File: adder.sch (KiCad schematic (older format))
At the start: 31 parts

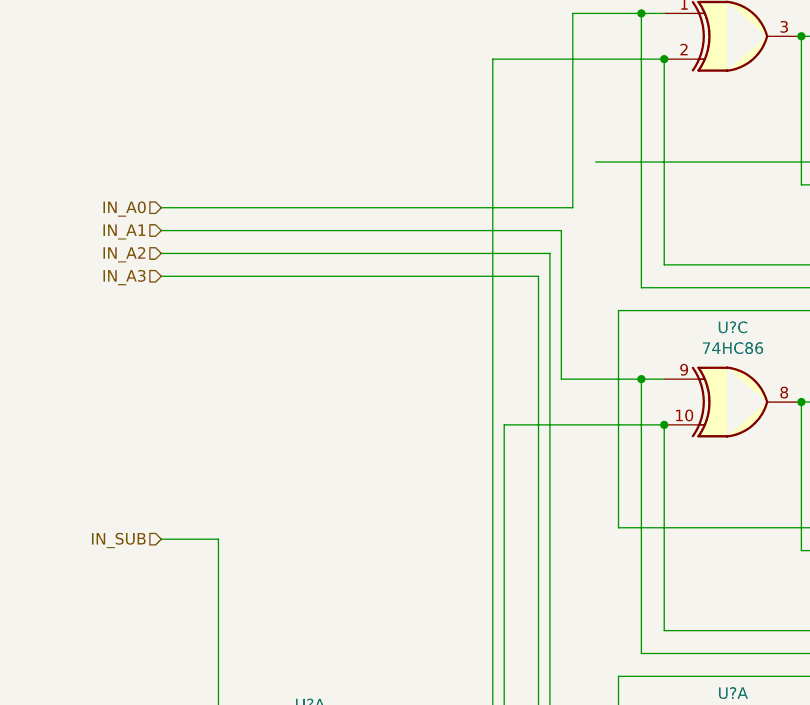
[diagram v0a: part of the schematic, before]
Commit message: Add missing wire in adder
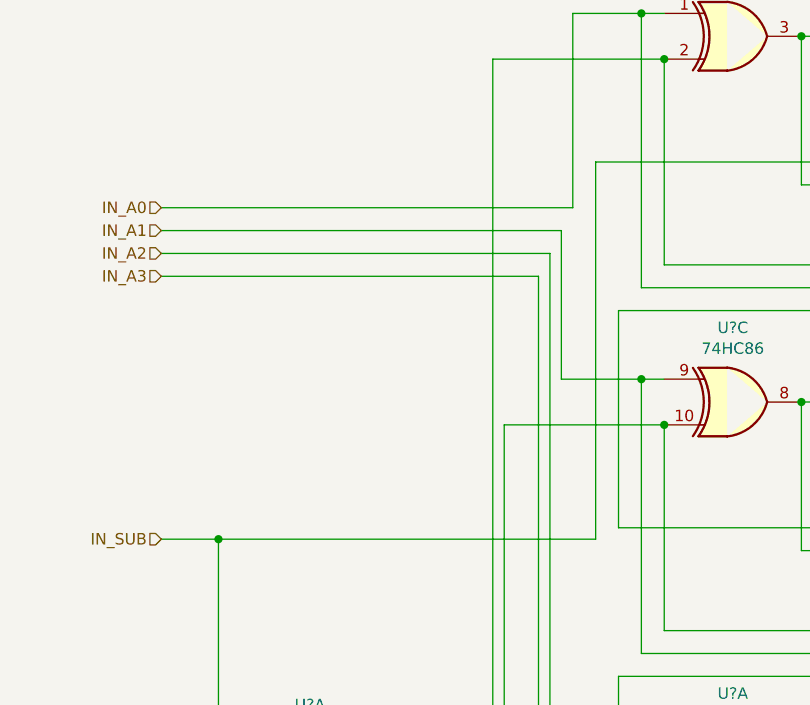
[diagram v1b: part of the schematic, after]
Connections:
- net IN_SUB: now also U?.1 (1A), U?.5
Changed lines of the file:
@@
 	1    0    0    -1
 $EndComp
+Wire Wire Line
+	2650 3500 4300 3500
+Wire Wire Line
+	4300 3500 4300 1850
+Connection ~ 2650 3500
 $EndSCHEMATC

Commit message: Anotate alu
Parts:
- gave numbers to parts that had none: 6

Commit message: tiny fixes in annotation
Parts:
- added unit 5 of U16
- gave numbers to parts that had none: 1
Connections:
- net +5V: now also U16.14 (VCC)
- net GND: now also U16.7 (GND)
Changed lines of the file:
@@
 AR Path="/6085805F" Ref="#PWR?"  Part="1"
 AR Path="/5FEB4D4D/6085805F" Ref="#PWR?"  Part="1"
-AR Path="/600A4AF3/600A5215/6085805F" Ref="#PWR?"  Part="1"
-F 0 "#PWR?" H 7600 2000 50  0001 C CNN
+AR Path="/600A4AF3/600A5215/6085805F" Ref="#PWR0112"  Part="1"
+F 0 "#PWR0112" H 7600 2000 50  0001 C CNN
 F 1 "GND" V 7605 2122 50  0000 R CNN
 F 2 "" H 7600 2250 50  0001 C CNN
@@
 AR Path="/60858065" Ref="#PWR?"  Part="1"
 AR Path="/5FEB4D4D/60858065" Ref="#PWR?"  Part="1"
-AR Path="/600A4AF3/600A5215/60858065" Ref="#PWR?"  Part="1"
-F 0 "#PWR?" H 7600 1100 50  0001 C CNN
+AR Path="/600A4AF3/600A5215/60858065" Ref="#PWR0115"  Part="1"
+F 0 "#PWR0115" H 7600 1100 50  0001 C CNN
 F 1 "+5V" V 7615 1378 50  0000 L CNN
 F 2 "" H 7600 1250 50  0001 C CNN
@@
 AR Path="/60858072" Ref="#PWR?"  Part="1"
 AR Path="/5FEB4D4D/60858072" Ref="#PWR?"  Part="1"
-AR Path="/600A4AF3/600A5215/60858072" Ref="#PWR?"  Part="1"
-F 0 "#PWR?" H 9000 2800 50  0001 C CNN
+AR Path="/600A4AF3/600A5215/60858072" Ref="#PWR0116"  Part="1"
+F 0 "#PWR0116" H 9000 2800 50  0001 C CNN
 F 1 "GND" V 9005 2922 50  0000 R CNN
 F 2 "" H 9000 3050 50  0001 C CNN
@@
 AR Path="/60858078" Ref="#PWR?"  Part="1"
 AR Path="/5FEB4D4D/60858078" Ref="#PWR?"  Part="1"
-AR Path="/600A4AF3/600A5215/60858078" Ref="#PWR?"  Part="1"
-F 0 "#PWR?" H 9000 1900 50  0001 C CNN
+AR Path="/600A4AF3/600A5215/60858078" Ref="#PWR0117"  Part="1"
+F 0 "#PWR0117" H 9000 1900 50  0001 C CNN
 F 1 "+5V" V 9015 2178 50  0000 L CNN
 F 2 "" H 9000 2050 50  0001 C CNN
@@
 AR Path="/6085808C" Ref="#PWR?"  Part="1"
 AR Path="/5FEB4D4D/6085808C" Ref="#PWR?"  Part="1"
-AR Path="/600A4AF3/600A5215/6085808C" Ref="#PWR?"  Part="1"
-F 0 "#PWR?" H 7850 3950 50  0001 C CNN
+AR Path="/600A4AF3/600A5215/6085808C" Ref="#PWR0118"  Part="1"
+F 0 "#PWR0118" H 7850 3950 50  0001 C CNN
 F 1 "GND" V 7855 4072 50  0000 R CNN
 F 2 "" H 7850 4200 50  0001 C CNN
@@
 AR Path="/60858092" Ref="#PWR?"  Part="1"
 AR Path="/5FEB4D4D/60858092" Ref="#PWR?"  Part="1"
-AR Path="/600A4AF3/600A5215/60858092" Ref="#PWR?"  Part="1"
-F 0 "#PWR?" H 7850 3350 50  0001 C CNN
+AR Path="/600A4AF3/600A5215/60858092" Ref="#PWR0120"  Part="1"
+F 0 "#PWR0120" H 7850 3350 50  0001 C CNN
 F 1 "+5V" V 7865 3628 50  0000 L CNN
 F 2 "" H 7850 3500 50  0001 C CNN
@@
 AR Path="/608B570A" Ref="#PWR?"  Part="1"
 AR Path="/5FEB4D4D/608B570A" Ref="#PWR?"  Part="1"
-AR Path="/600A4AF3/600A5215/608B570A" Ref="#PWR?"  Part="1"
-F 0 "#PWR?" H 8300 5200 50  0001 C CNN
+AR Path="/600A4AF3/600A5215/608B570A" Ref="#PWR0135"  Part="1"
+F 0 "#PWR0135" H 8300 5200 50  0001 C CNN
 F 1 "GND" V 8305 5322 50  0000 R CNN
 F 2 "" H 8300 5450 50  0001 C CNN
@@
 AR Path="/608B5710" Ref="#PWR?"  Part="1"
 AR Path="/5FEB4D4D/608B5710" Ref="#PWR?"  Part="1"
-AR Path="/600A4AF3/600A5215/608B5710" Ref="#PWR?"  Part="1"
-F 0 "#PWR?" H 8300 4300 50  0001 C CNN
+AR Path="/600A4AF3/600A5215/608B5710" Ref="#PWR0136"  Part="1"
+F 0 "#PWR0136" H 8300 4300 50  0001 C CNN
 F 1 "+5V" V 8315 4578 50  0000 L CNN
 F 2 "" H 8300 4450 50  0001 C CNN
@@
 AR Path="/608BBB4D" Ref="#PWR?"  Part="1"
 AR Path="/5FEB4D4D/608BBB4D" Ref="#PWR?"  Part="1"
-AR Path="/600A4AF3/600A5215/608BBB4D" Ref="#PWR?"  Part="1"
-F 0 "#PWR?" H 1700 6500 50  0001 C CNN
+AR Path="/600A4AF3/600A5215/608BBB4D" Ref="#PWR0137"  Part="1"
+F 0 "#PWR0137" H 1700 6500 50  0001 C CNN
 F 1 "GND" V 1705 6622 50  0000 R CNN
 F 2 "" H 1700 6750 50  0001 C CNN
@@
 AR Path="/608BBB53" Ref="#PWR?"  Part="1"
 AR Path="/5FEB4D4D/608BBB53" Ref="#PWR?"  Part="1"
-AR Path="/600A4AF3/600A5215/608BBB53" Ref="#PWR?"  Part="1"
-F 0 "#PWR?" H 1700 5600 50  0001 C CNN
+AR Path="/600A4AF3/600A5215/608BBB53" Ref="#PWR0138"  Part="1"
+F 0 "#PWR0138" H 1700 5600 50  0001 C CNN
 F 1 "+5V" V 1715 5878 50  0000 L CNN
 F 2 "" H 1700 5750 50  0001 C CNN
@@
 AR Path="/608E9FF4" Ref="#PWR?"  Part="1"
 AR Path="/5FEB4D4D/608E9FF4" Ref="#PWR?"  Part="1"
-AR Path="/600A4AF3/600A5215/608E9FF4" Ref="#PWR?"  Part="1"
-F 0 "#PWR?" H 9050 5050 50  0001 C CNN
+AR Path="/600A4AF3/600A5215/608E9FF4" Ref="#PWR0139"  Part="1"
+F 0 "#PWR0139" H 9050 5050 50  0001 C CNN
 F 1 "GND" V 9055 5172 50  0000 R CNN
 F 2 "" H 9050 5300 50  0001 C CNN
@@
 AR Path="/608E9FFA" Ref="#PWR?"  Part="1"
 AR Path="/5FEB4D4D/608E9FFA" Ref="#PWR?"  Part="1"
-AR Path="/600A4AF3/600A5215/608E9FFA" Ref="#PWR?"  Part="1"
-F 0 "#PWR?" H 9050 4150 50  0001 C CNN
+AR Path="/600A4AF3/600A5215/608E9FFA" Ref="#PWR0140"  Part="1"
+F 0 "#PWR0140" H 9050 4150 50  0001 C CNN
 F 1 "+5V" V 9065 4428 50  0000 L CNN
 F 2 "" H 9050 4300 50  0001 C CNN
@@
 P 7100 5650
 AR Path="/5FEB4D4D/600EFDE5" Ref="U?"  Part="2"
-AR Path="/600A4AF3/600A5215/600EFDE5" Ref="U?"  Part="4"
-F 0 "U?" H 7100 5975 50  0000 C CNN
+AR Path="/600A4AF3/600A5215/600EFDE5" Ref="U16"  Part="4"
+F 0 "U16" H 7100 5975 50  0000 C CNN
 F 1 "74HC86" H 7100 5884 50  0000 C CNN
 F 2 "Package_SO:TSSOP-14_4.4x5mm_P0.65mm" H 7100 5650 50  0001 C CNN
@@
 	4300 3500 4300 1850
 Connection ~ 2650 3500
+$Comp
+L power:GND #PWR?
+U 1 1 60384320
+P 10150 4200
+AR Path="/60384320" Ref="#PWR?"  Part="1"
+AR Path="/5FEB4D4D/60384320" Ref="#PWR?"  Part="1"
+AR Path="/600A4AF3/600A5215/60384320" Ref="#PWR0200"  Part="1"
+F 0 "#PWR0200" H 10150 3950 50  0001 C CNN
+F 1 "GND" V 10155 4072 50  0000 R CNN
+F 2 "" H 10150 4200 50  0001 C CNN
+F 3 "" H 10150 4200 50  0001 C CNN
+	1    10150 4200
+	1    0    0    -1
+$EndComp
+$Comp
+L power:+5V #PWR?
+U 1 1 60384326
+P 10150 3200
+AR Path="/60384326" Ref="#PWR?"  Part="1"
+AR Path="/5FEB4D4D/60384326" Ref="#PWR?"  Part="1"
+AR Path="/600A4AF3/600A5215/60384326" Ref="#PWR0201"  Part="1"
+F 0 "#PWR0201" H 10150 3050 50  0001 C CNN
+F 1 "+5V" V 10165 3328 50  0000 L CNN
+F 2 "" H 10150 3200 50  0001 C CNN
+F 3 "" H 10150 3200 50  0001 C CNN
+	1    10150 3200
+	1    0    0    -1
+$EndComp
+$Comp
+L 74xx:74HC86 U?
+U 5 1 6038432D
+P 10150 3700
+AR Path="/5FEB4D4D/6038432D" Ref="U?"  Part="5"
+AR Path="/600A4AF3/600A5215/6038432D" Ref="U16"  Part="5"
+F 0 "U16" H 10380 3746 50  0000 L CNN
+F 1 "74HC86" H 10380 3655 50  0000 L CNN
+F 2 "Package_SO:TSSOP-14_4.4x5mm_P0.65mm" H 10150 3700 50  0001 C CNN
+F 3 "https://datasheet.lcsc.com/szlcsc/Texas-Instruments-TI-SN74AHC86PWR_C117522.pdf" H 10150 3700 50  0001 C CNN
+F 4 "C117522" H 10150 3700 50  0001 C CNN "LCSC"
+	5    10150 3700
+	1    0    0    -1
+$EndComp
 $EndSCHEMATC

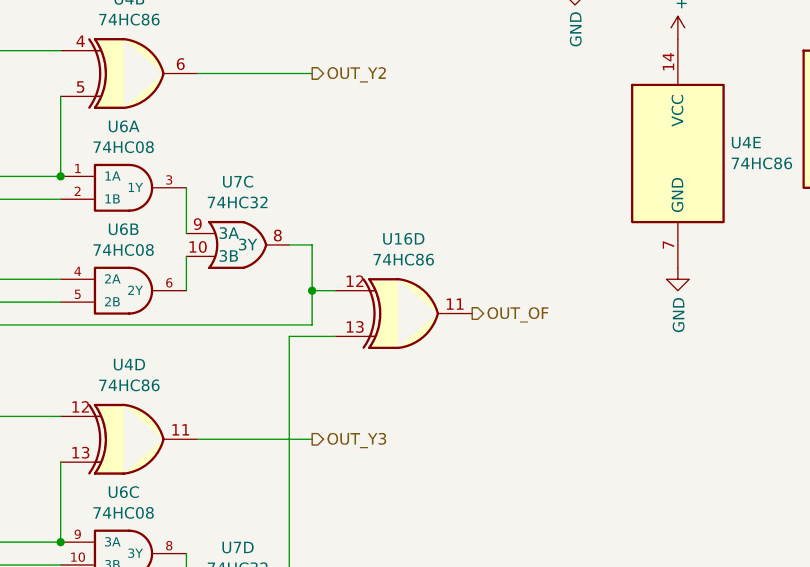
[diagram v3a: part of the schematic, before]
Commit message: exchanged a single AND
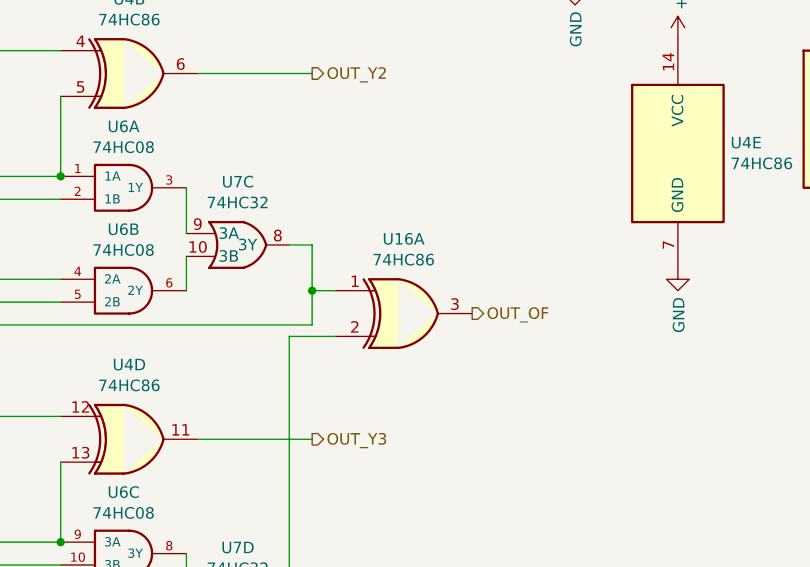
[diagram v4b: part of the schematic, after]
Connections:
- net OUT_OF: now also U16.3; no longer U16.11
- net at U4.13, U6.9 (3A), U7.8 (3Y): now also U16.1; no longer U16.12
- net at U7.11 (4Y): now also U16.2; no longer U16.13
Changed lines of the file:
@@
 $Comp
 L 74xx:74HC86 U?
-U 4 1 600EFDE5
+U 1 1 600EFDE5
 P 7100 5650
 AR Path="/5FEB4D4D/600EFDE5" Ref="U?"  Part="2"
-AR Path="/600A4AF3/600A5215/600EFDE5" Ref="U16"  Part="4"
+AR Path="/600A4AF3/600A5215/600EFDE5" Ref="U16"  Part="1"
 F 0 "U16" H 7100 5975 50  0000 C CNN
 F 1 "74HC86" H 7100 5884 50  0000 C CNN
@@
 F 3 "https://datasheet.lcsc.com/szlcsc/Texas-Instruments-TI-SN74AHC86PWR_C117522.pdf" H 7100 5650 50  0001 C CNN
 F 4 "C117522" H 7100 5650 50  0001 C CNN "LCSC"
-	4    7100 5650
+	1    7100 5650
 	1    0    0    -1
 $EndComp

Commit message: fixed some footprints
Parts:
- U5, U6, U7: footprint Housings_SOIC:SOIC-14_3.9x8.7mm_Pitch1.27mm -> Package_SO:SOIC-14_3.9x8.7mm_P1.27mm
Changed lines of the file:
@@
 F 0 "U6" H 5875 6967 50  0000 C CNN
 F 1 "74HC08" H 5875 6876 50  0000 C CNN
-F 2 "Housings_SOIC:SOIC-14_3.9x8.7mm_Pitch1.27mm" H 5850 6700 50  0001 C CNN
+F 2 "Package_SO:SOIC-14_3.9x8.7mm_P1.27mm" H 5850 6700 50  0001 C CNN
 F 3 "https://datasheet.lcsc.com/szlcsc/Nexperia-74HC08D-653_C5593.pdf" H 5850 6700 50  0001 C CNN
 F 4 "C5593" H 5850 6700 50  0001 C CNN "LCSC"
@@
 F 0 "U5" H 5875 3767 50  0000 C CNN
 F 1 "74HC08" H 5875 3676 50  0000 C CNN
-F 2 "Housings_SOIC:SOIC-14_3.9x8.7mm_Pitch1.27mm" H 5850 3500 50  0001 C CNN
+F 2 "Package_SO:SOIC-14_3.9x8.7mm_P1.27mm" H 5850 3500 50  0001 C CNN
 F 3 "https://datasheet.lcsc.com/szlcsc/Nexperia-74HC08D-653_C5593.pdf" H 5850 3500 50  0001 C CNN
 F 4 "C5593" H 5850 3500 50  0001 C CNN "LCSC"
@@
 F 0 "U7" H 6375 4025 50  0000 C CNN
 F 1 "74HC32" H 6375 3934 50  0000 C CNN
-F 2 "Housings_SOIC:SOIC-14_3.9x8.7mm_Pitch1.27mm" H 5850 3950 50  0001 C CNN
+F 2 "Package_SO:SOIC-14_3.9x8.7mm_P1.27mm" H 5850 3950 50  0001 C CNN
 F 3 "https://datasheet.lcsc.com/szlcsc/Nexperia-74HC32D-653_C5632.pdf" H 5850 3950 50  0001 C CNN
 F 4 "C5632" H 6400 3750 50  0001 C CNN "LCSC"
@@
 F 0 "U7" H 6375 2425 50  0000 C CNN
 F 1 "74HC32" H 6375 2334 50  0000 C CNN
-F 2 "Housings_SOIC:SOIC-14_3.9x8.7mm_Pitch1.27mm" H 5850 2350 50  0001 C CNN
+F 2 "Package_SO:SOIC-14_3.9x8.7mm_P1.27mm" H 5850 2350 50  0001 C CNN
 F 3 "https://datasheet.lcsc.com/szlcsc/Nexperia-74HC32D-653_C5632.pdf" H 5850 2350 50  0001 C CNN
 F 4 "C5632" H 6400 2150 50  0001 C CNN "LCSC"
@@
 F 0 "U5" H 5875 2617 50  0000 C CNN
 F 1 "74HC08" H 5875 2526 50  0000 C CNN
-F 2 "Housings_SOIC:SOIC-14_3.9x8.7mm_Pitch1.27mm" H 5850 2350 50  0001 C CNN
+F 2 "Package_SO:SOIC-14_3.9x8.7mm_P1.27mm" H 5850 2350 50  0001 C CNN
 F 3 "https://datasheet.lcsc.com/szlcsc/Nexperia-74HC08D-653_C5593.pdf" H 5850 2350 50  0001 C CNN
 F 4 "C5593" H 5850 2350 50  0001 C CNN "LCSC"
@@
 F 0 "U5" H 5875 2167 50  0000 C CNN
 F 1 "74HC08" H 5875 2076 50  0000 C CNN
-F 2 "Housings_SOIC:SOIC-14_3.9x8.7mm_Pitch1.27mm" H 5850 1900 50  0001 C CNN
+F 2 "Package_SO:SOIC-14_3.9x8.7mm_P1.27mm" H 5850 1900 50  0001 C CNN
 F 3 "https://datasheet.lcsc.com/szlcsc/Nexperia-74HC08D-653_C5593.pdf" H 5850 1900 50  0001 C CNN
 F 4 "C5593" H 5850 1900 50  0001 C CNN "LCSC"
@@
 F 0 "U6" H 5875 5817 50  0000 C CNN
 F 1 "74HC08" H 5875 5726 50  0000 C CNN
-F 2 "Housings_SOIC:SOIC-14_3.9x8.7mm_Pitch1.27mm" H 5850 5550 50  0001 C CNN
+F 2 "Package_SO:SOIC-14_3.9x8.7mm_P1.27mm" H 5850 5550 50  0001 C CNN
 F 3 "https://datasheet.lcsc.com/szlcsc/Nexperia-74HC08D-653_C5593.pdf" H 5850 5550 50  0001 C CNN
 F 4 "C5593" H 5850 5550 50  0001 C CNN "LCSC"
@@
 F 0 "U6" H 5875 5367 50  0000 C CNN
 F 1 "74HC08" H 5875 5276 50  0000 C CNN
-F 2 "Housings_SOIC:SOIC-14_3.9x8.7mm_Pitch1.27mm" H 5850 5100 50  0001 C CNN
+F 2 "Package_SO:SOIC-14_3.9x8.7mm_P1.27mm" H 5850 5100 50  0001 C CNN
 F 3 "https://datasheet.lcsc.com/szlcsc/Nexperia-74HC08D-653_C5593.pdf" H 5850 5100 50  0001 C CNN
 F 4 "C5593" H 5850 5100 50  0001 C CNN "LCSC"
@@
 F 0 "U5" H 9230 2596 50  0000 L CNN
 F 1 "74HC08" H 9230 2505 50  0000 L CNN
-F 2 "Housings_SOIC:SOIC-14_3.9x8.7mm_Pitch1.27mm" H 9000 2550 50  0001 C CNN
+F 2 "Package_SO:SOIC-14_3.9x8.7mm_P1.27mm" H 9000 2550 50  0001 C CNN
 F 3 "https://datasheet.lcsc.com/szlcsc/Nexperia-74HC08D-653_C5593.pdf" H 9000 2550 50  0001 C CNN
 F 4 "C5593" H 9000 2550 50  0001 C CNN "LCSC"
@@
 F 0 "U7" H 8028 3896 50  0000 L CNN
 F 1 "74HC32" H 8028 3805 50  0000 L CNN
-F 2 "Housings_SOIC:SOIC-14_3.9x8.7mm_Pitch1.27mm" H 7600 4050 50  0001 C CNN
+F 2 "Package_SO:SOIC-14_3.9x8.7mm_P1.27mm" H 7600 4050 50  0001 C CNN
 F 3 "https://datasheet.lcsc.com/szlcsc/Nexperia-74HC32D-653_C5632.pdf" H 7600 4050 50  0001 C CNN
 F 4 "C5632" H 8150 3850 50  0001 C CNN "LCSC"
@@
 F 0 "U6" H 9280 4846 50  0000 L CNN
 F 1 "74HC08" H 9280 4755 50  0000 L CNN
-F 2 "Housings_SOIC:SOIC-14_3.9x8.7mm_Pitch1.27mm" H 9050 4800 50  0001 C CNN
+F 2 "Package_SO:SOIC-14_3.9x8.7mm_P1.27mm" H 9050 4800 50  0001 C CNN
 F 3 "https://datasheet.lcsc.com/szlcsc/Nexperia-74HC08D-653_C5593.pdf" H 9050 4800 50  0001 C CNN
 F 4 "C5593" H 9050 4800 50  0001 C CNN "LCSC"
@@
 F 0 "U6" H 5875 7417 50  0000 C CNN
 F 1 "74HC08" H 5875 7326 50  0000 C CNN
-F 2 "Housings_SOIC:SOIC-14_3.9x8.7mm_Pitch1.27mm" H 5850 7150 50  0001 C CNN
+F 2 "Package_SO:SOIC-14_3.9x8.7mm_P1.27mm" H 5850 7150 50  0001 C CNN
 F 3 "https://datasheet.lcsc.com/szlcsc/Nexperia-74HC08D-653_C5593.pdf" H 5850 7150 50  0001 C CNN
 F 4 "C5593" H 5850 7150 50  0001 C CNN "LCSC"
@@
 F 0 "U7" H 6375 7225 50  0000 C CNN
 F 1 "74HC32" H 6375 7134 50  0000 C CNN
-F 2 "Housings_SOIC:SOIC-14_3.9x8.7mm_Pitch1.27mm" H 5850 7150 50  0001 C CNN
+F 2 "Package_SO:SOIC-14_3.9x8.7mm_P1.27mm" H 5850 7150 50  0001 C CNN
 F 3 "https://datasheet.lcsc.com/szlcsc/Nexperia-74HC32D-653_C5632.pdf" H 5850 7150 50  0001 C CNN
 F 4 "C5632" H 6400 6950 50  0001 C CNN "LCSC"
@@
 F 0 "U5" H 5875 4217 50  0000 C CNN
 F 1 "74HC08" H 5875 4126 50  0000 C CNN
-F 2 "Housings_SOIC:SOIC-14_3.9x8.7mm_Pitch1.27mm" H 5850 3950 50  0001 C CNN
+F 2 "Package_SO:SOIC-14_3.9x8.7mm_P1.27mm" H 5850 3950 50  0001 C CNN
 F 3 "https://datasheet.lcsc.com/szlcsc/Nexperia-74HC08D-653_C5593.pdf" H 5850 3950 50  0001 C CNN
 F 4 "C5593" H 5850 3950 50  0001 C CNN "LCSC"
@@
 F 0 "U7" H 6375 5625 50  0000 C CNN
 F 1 "74HC32" H 6375 5534 50  0000 C CNN
-F 2 "Housings_SOIC:SOIC-14_3.9x8.7mm_Pitch1.27mm" H 5850 5550 50  0001 C CNN
+F 2 "Package_SO:SOIC-14_3.9x8.7mm_P1.27mm" H 5850 5550 50  0001 C CNN
 F 3 "https://datasheet.lcsc.com/szlcsc/Nexperia-74HC32D-653_C5632.pdf" H 5850 5550 50  0001 C CNN
 F 4 "C5632" H 6400 5350 50  0001 C CNN "LCSC"
